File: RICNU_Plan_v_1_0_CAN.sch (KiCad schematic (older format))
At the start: 4 parts, among them U5 TCAN334G

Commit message: had to relocate 4.7uF cap for STM32 based on datasheet info. Experimenting with reset button location
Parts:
- added R95: 10k, Resistors_SMD:R_0402_NoSilk, symbol R
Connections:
- net +3V3: now also R95.1
- net CAN.TX: now also R95.2
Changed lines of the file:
@@
 Text Label 5300 3650 2    60   ~ 0
 CAN_VCC
+$Comp
+L R R95
+U 1 1 5A21C74B
+P 5500 3200
+F 0 "R95" V 5580 3200 50  0000 C CNN
+F 1 "10k" V 5500 3200 50  0000 C CNN
+F 2 "Resistors_SMD:R_0402_NoSilk" V 5430 3200 50  0001 C CNN
+F 3 "" H 5500 3200 50  0001 C CNN
+	1    5500 3200
+	1    0    0    -1
+$EndComp
+Wire Wire Line
+	5500 3450 5500 3350
+Connection ~ 5500 3450
+Wire Wire Line
+	5500 3050 5500 2950
+$Comp
+L +3V3 #PWR036
+U 1 1 5A21C7C4
+P 5500 2950
+F 0 "#PWR036" H 5500 2800 50  0001 C CNN
+F 1 "+3V3" H 5500 3090 50  0000 C CNN
+F 2 "" H 5500 2950 50  0001 C CNN
+F 3 "" H 5500 2950 50  0001 C CNN
+	1    5500 2950
+	1    0    0    -1
+$EndComp
 $EndSCHEMATC

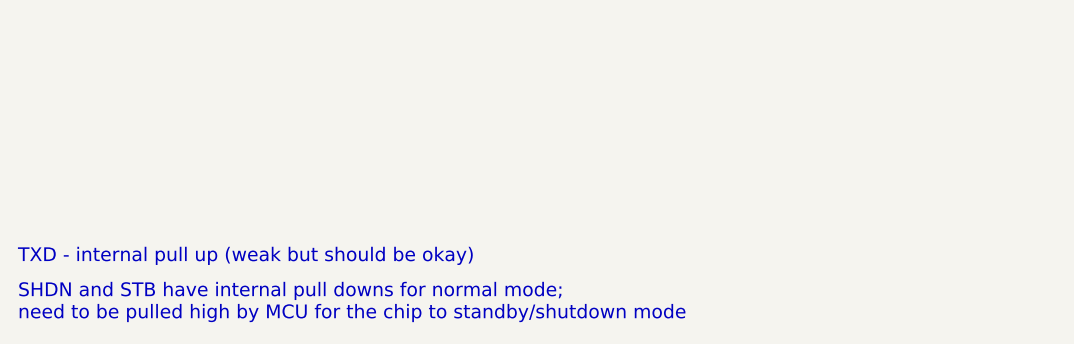
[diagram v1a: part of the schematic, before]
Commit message: Deleting PDFs
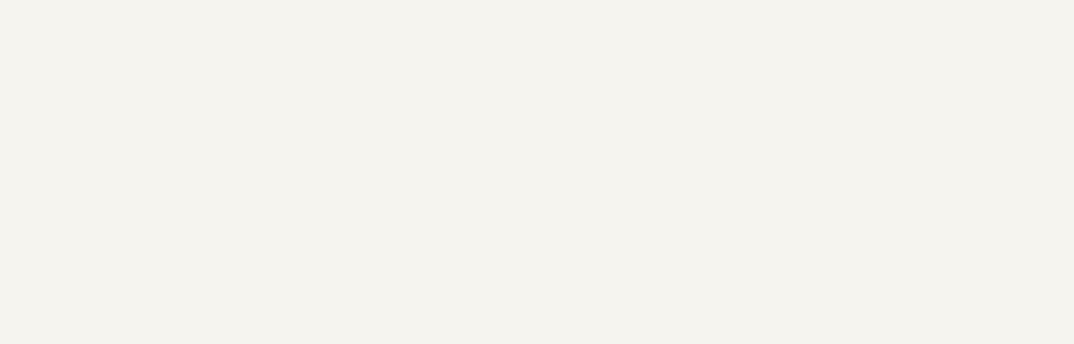
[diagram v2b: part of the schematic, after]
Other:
- note removed: "SHDN and STB have internal pull downs for normal mode;\nneed to be pulled high by MCU for the chip to standby/shutdown mode"
- note removed: "TXD - internal pull up (weak but should be okay)"
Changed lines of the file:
@@
 	1    0    0    -1
 $EndComp
-Text Notes 1050 7200 0    60   ~ 0
-SHDN and STB have internal pull downs for normal mode;\nneed to be pulled high by MCU for the chip to standby/shutdown mode
-Text Notes 1050 6950 0    60   ~ 0
-TXD - internal pull up (weak but should be okay)
 $Comp
 L GND #PWR034
